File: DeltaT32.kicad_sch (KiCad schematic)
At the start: 35 parts, among them J1 PH2.0, J2 USB_C_Receptacle_USB2.0_16P, J3 SH1.0, Q1 AO3401A, SW1 Boot, SW2 Reset, SW3 SW_SPDT_312, U1 TP4057, U2 MPU-6050, U3 ESP32-C3-MINI-1, U4 AP2112K-3.3

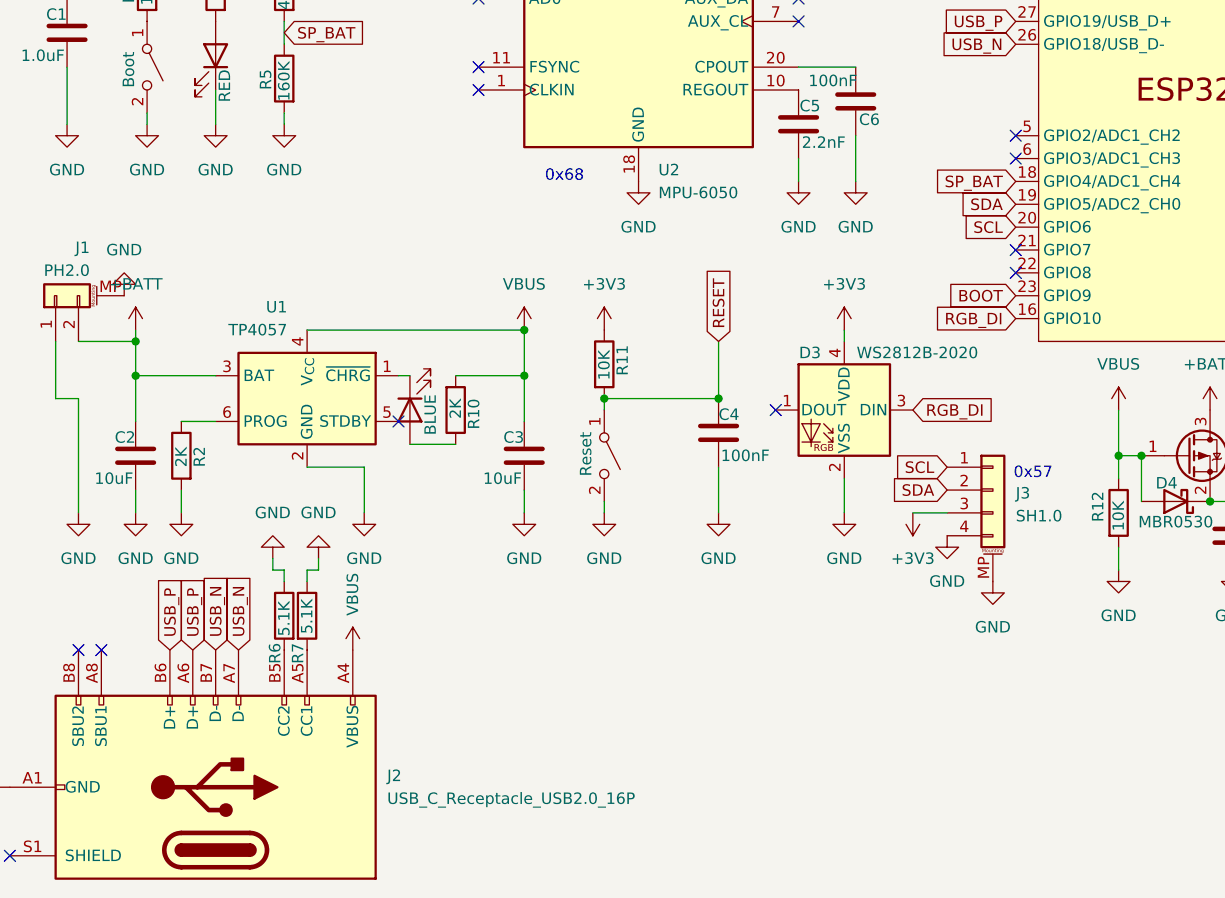
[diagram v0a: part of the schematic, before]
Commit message: Up
Upgrade kicad version
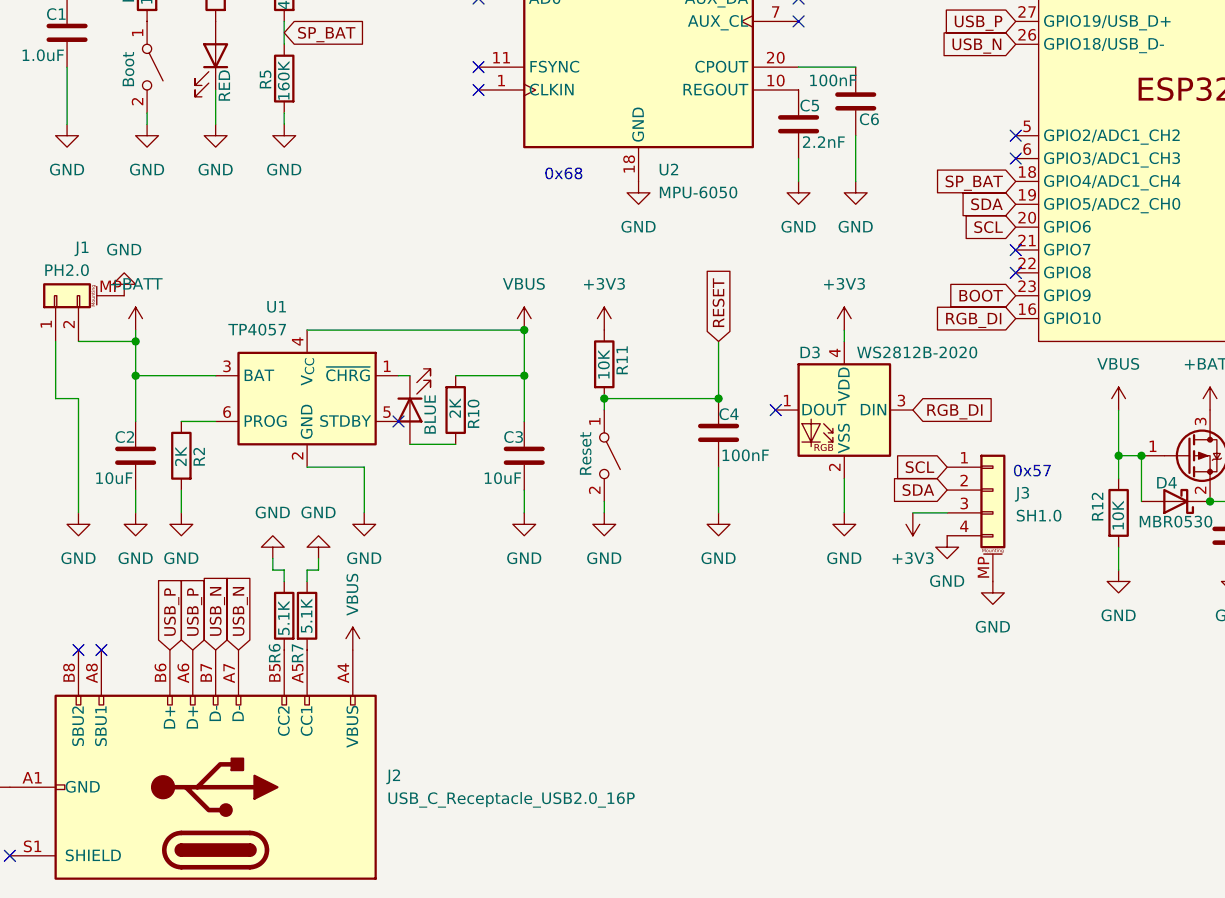
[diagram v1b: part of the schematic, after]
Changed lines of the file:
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@@
 (kicad_sch
-	(version 20231120)
+	(version 20250114)
 	(generator "eeschema")
-	(generator_version "8.0")
+	(generator_version "9.0")
 	(paper "A5")
+	(text_box "0x57"
+		(exclude_from_sim no)
+		(at 129.54 85.09 0)
+		(size 0 0)
+		(margins 0.9525 0.9525 0.9525 0.9525)
+		(stroke
+			(width 0)
+			(type default)
+		)
+		(fill
+			(type none)
+		)
+		(effects
+			(font
+				(size 1.27 1.27)
+			)
+			(justify left top)
+		)
+	)
+	(text_box "0x68"
+		(exclude_from_sim no)
+		(at 77.47 52.07 0)
+		(size 0 0)
+		(margins 0.9525 0.9525 0.9525 0.9525)
+		(stroke
+			(width 0)
+			(type default)
+		)
+		(fill
+			(type none)
+		)
+		(effects
+			(font
+				(size 1.27 1.27)
+			)
+			(justify left top)
+		)
+	)
 	(junction
 		(at 91.44 19.05)
@@
 		)
 	)
-	(text_box "0x57"
-		(exclude_from_sim no)
-		(at 129.54 85.09 0)
-		(size 0 0)
-		(stroke
-			(width 0)
-			(type default)
-		)
-		(fill
-			(type none)
-		)
-		(effects
-			(font
-				(size 1.27 1.27)
-			)
-			(justify left top)
-		)
-	)
-	(text_box "0x68"
-		(exclude_from_sim no)
-		(at 77.47 52.07 0)
-		(size 0 0)
-		(stroke
-			(width 0)
-			(type default)
-		)
-		(fill
-			(type none)
-		)
-		(effects
-			(font
-				(size 1.27 1.27)
-			)
-			(justify left top)
-		)
-	)
 	(global_label "SP_BAT"
 		(shape input)
@@
 		)
 	)
+	(embedded_fonts no)
 )

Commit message: Update Board
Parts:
- removed C1, C7, C8, C9: 1.0uF, Capacitor_SMD:C_0402_1005Metric, symbol Device:C
- removed C2, C3: 10uF, Capacitor_SMD:C_0402_1005Metric, symbol Device:C
- removed C4, C6: 100nF, Capacitor_SMD:C_0402_1005Metric, symbol Device:C
- removed C5: 2.2nF, Capacitor_SMD:C_0603_1608Metric, symbol Device:C
- removed D1: RED, LED_SMD:LED_0402_1005Metric, symbol Device:LED
- removed D2: BLUE, LED_SMD:LED_0402_1005Metric, symbol Device:LED
- removed D3: WS2812B-2020, LED_SMD:LED_WS2812B-2020_PLCC4_2.0x2.0mm, symbol LED:WS2812B-2020
- removed D4: MBR0530, Diode_SMD:D_SOD-123, symbol Diode:MBR0530
- removed J1: PH2.0, Connector_JST:JST_PH_B2B-PH-SM4-TB_1x02-1MP_P2.00mm_Vertical, symbol Connector_Generic_MountingPin:Conn_01x02_MountingPin
- removed J3: SH1.0, Connector_JST:JST_SH_BM04B-SRSS-TB_1x04-1MP_P1.00mm_Vertical, symbol Connector_Generic_MountingPin:Conn_01x04_MountingPin
- removed Q1: AO3401A, Package_TO_SOT_SMD:SOT-23, symbol Transistor_FET:AO3401A
- removed R11, R12: 10K, Resistor_SMD:R_0402_1005Metric, symbol Device:R
- removed SW1: Boot, Button_Switch_SMD:SW_Push_SPST_NO_Alps_SKRK, symbol Switch:SW_SPST
- removed SW2: Reset, Button_Switch_SMD:SW_Push_SPST_NO_Alps_SKRK, symbol Switch:SW_SPST
- removed SW3: SW_SPDT_312, Button_Switch_SMD:SW_SPDT_PCM12, symbol Switch:SW_SPDT_312
- removed U1: TP4057, Package_TO_SOT_SMD:TSOT-23-6, symbol Battery_Management:TP4057
- removed U2: MPU-6050, Sensor_Motion:InvenSense_QFN-24_4x4mm_P0.5mm, symbol Sensor_Motion:MPU-6050
- removed U3: ESP32-C3-MINI-1, PCM_Espressif:ESP32-C3-MINI-1, symbol PCM_Espressif:ESP32-C3-MINI-1
- removed U4: AP2112K-3.3, Package_TO_SOT_SMD:SOT-23-5, symbol Regulator_Linear:AP2112K-3.3
- added C1: 10nF 10V, Capacitor_SMD:C_0402_1005Metric, symbol Device:C_Small
- added C10: 1nF 10V, Capacitor_SMD:C_0402_1005Metric, symbol Device:C_Small
- added C11, C12: DNP, Capacitor_SMD:C_0402_1005Metric, symbol Device:C_Small
- added C2: 100nF 10V, Capacitor_SMD:C_0402_1005Metric, symbol Device:C_Small
- added C3, C4: 1uF 16V, Capacitor_SMD:C_0402_1005Metric, symbol Device:C_Small
- added C5, C6: 4.7uF 16V, Capacitor_SMD:C_0603_1608Metric, symbol Device:C_Small
- added C7, C9: 10uF 16V, Capacitor_SMD:C_0805_2012Metric, symbol Device:C_Small
- added C8: 22pF 50V, Capacitor_SMD:C_0603_1608Metric, symbol Device:C_Small
- added D1: LESD8D3.3CAT5G, Diode_SMD:D_SOD-882, symbol Device:D_TVS
- added D2: WS2812B, LED_SMD:LED_WS2812B-2020_PLCC4_2.0x2.0mm, symbol LED:WS2812B
- added D3: BLUE LED, LED_SMD:LED_0603_1608Metric, symbol Device:LED
- added D4: RED LED, LED_SMD:LED_0603_1608Metric, symbol Device:LED
- added D5, D6, D8: LESD5D5.0CT1G, Diode_SMD:D_SOD-523, symbol Device:D_TVS
- added D7, D9: B5819W, Diode_SMD:D_SOD-123, symbol Device:D_Schottky
- added J1: JST SH 1.0, Connector_JST:JST_SH_SM04B-SRSS-TB_1x04-1MP_P1.00mm_Horizontal, symbol Connector_Generic_MountingPin:Conn_01x04_MountingPin
- added J2: JST PH 2.0, Connector_JST:JST_PH_B2B-PH-K_1x02_P2.00mm_Vertical, symbol Connector_Generic:Conn_01x02
- added L1: 2.2uH 2.2A, Inductor_SMD:L_Bourns-SRN4018, symbol Device:L
- added Q1: DMG3415U, Package_TO_SOT_SMD:SOT-23, symbol Transistor_FET:DMG2301L
- added R14, R7: 10K, Resistor_SMD:R_0402_1005Metric, symbol Device:R
- added R15, R5: 1K, Resistor_SMD:R_0402_1005Metric, symbol Device:R
- added R4, R8: 0R, Resistor_SMD:R_0402_1005Metric, symbol Device:R
- added R6: 470R, Resistor_SMD:R_0402_1005Metric, symbol Device:R
- added R9: 100K, Resistor_SMD:R_0402_1005Metric, symbol Device:R
- added SW1: MSK-12C02-07, Button_Switch_SMD:SW_SPDT_PCM12, symbol Switch:SW_SPDT_312
- added SW2: BOOT, Button_Switch_SMD:SW_Push_SPST_NO_Alps_SKRK, symbol Switch:SW_Push
- added SW3: RESET, Button_Switch_SMD:SW_Push_SPST_NO_Alps_SKRK, symbol Switch:SW_Push
- added TP1: TX, TestPoint:TestPoint_Pad_D1.0mm, symbol Connector:TestPoint
- added TP2: RX, TestPoint:TestPoint_Pad_D1.0mm, symbol Connector:TestPoint
- added TP3: IO3, TestPoint:TestPoint_Pad_D1.0mm, symbol Connector:TestPoint
- added TP4: IO5, TestPoint:TestPoint_Pad_D1.0mm, symbol Connector:TestPoint
- added TP5: IO6, TestPoint:TestPoint_Pad_D1.0mm, symbol Connector:TestPoint
- added U1: ESP32-C3-MINI-1, PCM_Espressif:ESP32-C3-MINI-1, symbol PCM_Espressif:ESP32-C3-MINI-1
- added U2: MCP73831T-2ACI/OT, Package_TO_SOT_SMD:SOT-23-5, symbol Battery_Management:MCP73831-2-OT
- added U3: SY8088, Package_TO_SOT_SMD:SOT-23-5, symbol Rust_Board:SY8088
- added Y1: 32.768Hz, Crystal:Crystal_SMD_3215-2Pin_3.2x1.5mm, symbol Device:Crystal
- J3: renamed from J2; value USB_C_Receptacle_USB2.0_16P -> USB C 16P; footprint Connector_USB:USB_C_Receptacle_GCT_USB4110 -> Connector_USB:USB_C_Receptacle_GCT_USB4105-xx-A_16P_TopMnt_Horizontal
- R1: value 10K -> 0R
- R10: value 2K -> 22K1
- R11: renamed from R6; value 5.1K -> 5K1
- R12: renamed from R7; value 5.1K -> 5K1
- R13: value 10K -> 100K
- R2, R3: value 2K -> 10K
- renumbered R4 to R16, R5 to R17
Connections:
- net +BATT: now also C6.1, J2.2 (Pin_2), Q1.3 (D), U2.3 (VBAT)
- net BOOT: now also C10.2, R14.2, SW3.1, U1.23 (GPIO9); no longer R1.1
- net GND: now also R10.2, R13.2, R3.2, C1.2, C10.1, C11.2, C12.2, C2.2, C3.2, C4.2, C5.1, C6.2, C7.2, C9.2, D1.2 (A2), D2.3 (VSS), D4.1 (K), D5.2 (A2), D6.2 (A2), D8.2 (A2), J1.1 (Pin_1), J2.1 (Pin_1), R8.1, SW2.2, SW3.2, U1.1 (GND), U1.11 (GND), U1.14 (GND), U1.2 (GND), U1.36 (GND), U1.37 (GND), U1.38 (GND), U1.39 (GND), U1.40 (GND), U1.41 (GND), U1.42 (GND), U1.43 (GND), U1.44 (GND), U1.45 (GND), U1.46 (GND), U1.47 (GND), U1.48 (GND), U1.49 (GND), U1.50 (GND), U1.51 (GND), U1.52 (GND), U1.53 (GND), U2.2 (VSS), U3.2 (GND); no longer R2.2
- net SCL: now also J1.3 (Pin_3), U1.22 (GPIO8)
- net SDA: now also J1.4 (Pin_4), U1.16 (GPIO10)
- net VBUS: now also R13.1, C5.2, D3.2 (A), D7.1 (K), D9.2 (A), Q1.1 (G), U2.4 (VDD); no longer J3.A4 (VBUS), J3.A9 (VBUS), J3.B4 (VBUS), J3.B9 (VBUS), R10.2
- net +3.3V: now reaches R2.1
- net +3.3V: now also C1.1, C2.1, C3.1, D1.1 (A1), D2.1 (VDD), J1.2 (Pin_2), R14.1, SW1.1 (B), U1.3 (3V3)
- net at R1.2: now also U1.6 (GPIO3/ADC1_CH3)
- net at R10.1: now also C8.2, R9.2, U3.5 (FB)
- net at J3.S1 (SHIELD): now also R8.2
- net +3V3: no longer names the net of R3.1
- net +3V3: now also U2.5 (PROG)
- net SP_BAT renamed IO3
- net IO3: now also R1.1
- net USB_N renamed USB_D-
- net USB_D-: now also D6.1 (A1), U1.26 (GPIO18/USB_D-)
- net USB_P renamed USB_D+
- net USB_D+: now also D5.1 (A1), U1.27 (GPIO19/USB_D+)
- new net: TP3.1, U1.18 (GPIO4/ADC1_CH4)
- new net: R5.1, U2.1 (STAT)
- new net: D3.1 (K), R5.2
- new net: D7.2 (A), D8.1 (A1), J3.A4 (VBUS), J3.A9 (VBUS), J3.B4 (VBUS), J3.B9 (VBUS)
- new net: D2.4 (DIN), R4.2
- new net: TP4.1, U1.19 (GPIO5/ADC2_CH0)
- new net: TP5.1, U1.20 (GPIO6)
- new net: TP2.1, U1.30 (GPIO20/U0RXD)
- new net: TP1.1, U1.31 (GPIO21/U0TXD)
- new net: D4.2 (A), R6.2
- new net +5V: C7.1, D9.1 (K), Q1.2 (S), R7.1, U3.4 (IN)
- new net Buck_Coil: L1.1, U3.3 (LX)
- new net CHIP_PU: C4.1, R2.2, SW2.1, U1.8 (EN/CHIP_PU)
- new net EN: R7.2, U3.1 (EN)
- new net IO0: C11.1, R15.1, U1.12 (GPIO0/ADC1_CH0/XTAL_32K_P), Y1.1
- new net IO1: C12.1, R15.2, U1.13 (GPIO1/ADC1_CH1/XTAL_32K_N), Y1.2
- new net IO2: R4.1, U1.5 (GPIO2/ADC1_CH2)
- new net IO7: R6.1, U1.21 (GPIO7)
- new net Switch: C8.1, C9.1, L1.2, R9.1, SW1.2 (C)
- no-connect marks 20 -> 5
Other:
- added sheet BMI (BMI.kicad_sch)
- added sheet ICM20948 (ICM20948.kicad_sch)
- added sheet MPU6050 (MPU6050.kicad_sch)
- added sheet MPU9250 (MPU9250.kicad_sch)
- note added: "Buck Converter 3V3 Rails"
- note added: "Buttons (Reset & Boot)"
- note added: "Charge Management Controller"
- note added: "ESP32-C3-MINI-1 Module"
- note added: "IMU & Heart Rate Sensor"
- note added: "IMU Default : 0x68 (1101000b) Alternative : 0x69 (1101001b) Heart-Rate Sensor Default : 0x57 (1010111b)"
- note added: "LED RED GPIO7 RGB GPIO2"
- note added: "LF Crystal 32.768Hz Do Not Populate"
- note added: "USB & Battery Switch"
- note added: "USB Type-C Connector"
- note added: "Voltage Divider"
- title: (none) -> DeltaT32
- moved on the sheet: J3, R11, R12, R16, R17

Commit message: Update Board
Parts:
- J2: footprint Connector_JST:JST_PH_B2B-PH-K_1x02_P2.00mm_Vertical -> Connector_JST:JST_PH_S2B-PH-K_1x02_P2.00mm_Horizontal
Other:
- removed sheet ICM20948
- removed sheet MPU6050
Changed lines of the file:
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@@
 	(polyline
 		(pts
-			(xy 64.77 102.87) (xy 64.77 156.21)
+			(xy 64.77 102.87) (xy 64.77 139.7)
 		)
 		(stroke
@@
 	(polyline
 		(pts
-			(xy 12.7 156.21) (xy 12.7 102.87)
+			(xy 12.7 139.7) (xy 12.7 102.87)
 		)
 		(stroke
@@
 	(polyline
 		(pts
-			(xy 64.77 156.21) (xy 12.7 156.21)
+			(xy 64.77 139.7) (xy 12.7 139.7)
 		)
 		(stroke
@@
 			"AAAAAAAAAAAAAAAAAAAAAAAAAAAAAAAAAAAAAAAAAAAAAAAAAAAAAADwAAAAAAAAAASzwJEABACA"
 			"0JgX/psBAACAvxj+mwEAAIC/GP6bAQAAABAAAAAAAAAAAAAAAAAAAICvGP6bAQAAAAAAAAAAAAAA"
-			"AAAAAAAAAAAAAAAAAAAAoK8Y/psBAAAAAAAAAAAAAAAAAAAAAAAAAAAAAAAAAADArxj+mw=="
+			"AAAAAAAAAAAAAAAAAAAAoK8Y/psBAAAAAAAAAAAAAAAAAAAAAAAAAAAAAAAAAADArxj+mwAAAAAA"
+			"AAAAAAAAAAAAAAAAAAAAAAAAAAAAAAAAAAAAAAAAAAAAAAAAAAAAAAAAAAAAAAAAAAAAAAAAAAAA"
+			"AAAAAAAAAAAAAAAAAAAAAAAAAAAAAAAAAAAAAAAAAAAAAAAAAAAAAAAAAAAAAAAAAAAAAAAAAAAA"
+			"AAAAAAAAAAAAAAAAAAAAAAAAAAAAAAAAAAAAAAAAAAAAAAAAAAAAAAAAAAAAAAAAAAAAAAAAAAAA"
+			"AAAAAAAAAAAAAAAAAAAAAAAAAAAAAAAAAAAAAAAAAAAAAAAAAAAAAAAAAAAAAAAAAAAAAAAAAAAA"
+			"AAAAAAAAAAAAAAAAAAAAAAAAAAAAAAAAAAAAAAAAAAAAAAAAAAAAAAAAAAAAAAAAAAAAAAAAAAAA"
+			"AAAAAAAAAAAAAAAAAAAAAAAAAAAAAAAAAAAAAAAAAAAAAAAAAAAAAAAAAAAAAAAAAAAAAAAAAAAA"
+			"AAAAAAAAAAAAAAAAAAAAAAAAAAAAAAAAAAAAAAAAAAAAAAAAAAAAAAAAAAAAAAAAAAAAAAAAAAAA"
+			"AAAAAAAAAAAAAAAAAAAAAAAAAAAAAAAAAAAAAAAAAAAAAAAAAAAAAAAAAAAAAAAAAAAAAAAAAAAA"
+			"AAAAAAAAAAAAAAAAAAAAAAAAAAAAAAAAAAAAAAAAAAAAAAAAAAAAAAAAAAAAAAAAAAAAAAAAAAAA"
+			"AAAAAAAAAAAAAAAAAAAAAAAAAAAAAAAAAAAAAAAAAAAAAAAAAAAAAAAAAAAAAAAAAAAAAAAAAAAA"
+			"AAAAAAAAAAAAAAAAAAAAAAAAAAAAAAAAAAAAAAAAAAAAAAAAAAAAAAAAAAAAAAAAAAAAAAAAAAAA"
+			"AAAAAAAAAAAAAAAAAAAAAAAAAAAAAAAAAAAAAAAAAAAAAAAAAAAAAAAAAAAAAAAAAAAAAAAAAAAA"
+			"AAAAAAAAAAAAAAAAAAAAAAAAAAAAAAAAAAAAAAAAAAAAAAAAAAAAAAAAAAAAAAAAAAAAAAAAAAAA"
+			"AAAAAAAAAAAAAAAAAAAAAAAAAAAAAAAAAAAAAAAAAAAAAAAAAAAAAAAAAAAAAAAAAAAAAAAAAAAA"
+			"AAAAAAAAAAAAAAAAAAAAAAAAAAAAAAAAAAAAAAAAAAAAAAAAAAAAAAAAAAAAAAAAAAAAAAAAAAAA"
+			"AAAAAAAAAAAAAAAAAAAAAAAAAAAAAAAAAAAAAAAAAAAAAAAAAAAAAAAAAAAAAAAAAAAAAAAAAAAA"
+			"AAAAAAAAAAAAAAAAAAAAAAAAAAAAAAAAAAAAAAAAAAAAAAAAAAAAAAAAAAAAAAAAAAAAAAAAAAAA"
+			"AAAAAAAAAAAAAAAAAAAAAAAAAAAAAAAAAAAAAAAAAAAAAAAAAAAAAAAAAAAAAAAAAAAAAAAAAAAA"
+			"AAAAAAAAAAAAAAAAAAAAAAAAAAAAAAAAAAAAAAAAAAAAAAAAAAAAAAAAAAAAAAAAAAAAAAAAAAAA"
+			"AAAAAAAAAAAAAAAAAAAAAAAAAAAAAAAAAAAAAAAAAAAAAAAAAAAAAAAAAAAAAAAAAAAAAAAAAAAA"
+			"AAAAAAAAAAAAAAAAAAAAAAAAAAAAAAAAAAAAAAAAAAAAAAAAAAAAAAAAAAAAAAAAAAAAAAAAAAAA"
+			"AAAAAAAAAAAAAAAAAAAAAAAAAAAAAAAAAAAAAAAAAAAAAAAAAAAAAAAAAAAAAAAAAAAAAAAAAAAA"
+			"AAAAAAAAAAAAAAAAAAAAAAAAAAAAAAAAAAAAAAAAAAAAAAAAAAAAAAAAAAAAAAAAAAAAAAAAAAAA"
+			"AAAAAAAAAAAAAAAAAAAAAAAAAAAAAAAAAAAAAAAAAAAAAAAAAAAAAAAAAAAAAAAAAAAAAAAAAAAA"
+			"AAAAAAAAAAAAAAAAAAAAAAAAAAAAAAAAAAAAAAAAAAAAAAAAAAAAAAAAAAAAAAAAAAAAAAAAAAAA"
+			"AAAAAAAAAAAAAAAAAAAAAAAAAAAAAAAAAAAAAAAAAAAAAAAAAAAAAAAAAAAAAAAAAAAAAAAAAAAA"
+			"AAAAAAAAAAAAAAAAAAAAAAAAAAAAAAAAAAAAAAAAAAAAAAAAAAAAAAAAAAAAAAAAAAAAAAAAAAAA"
+			"AAAAAAAAAAAAAAAAAAAAAAAAAAAAAAAAAAAAAAAAAAAAAAAAAAAAAAAAAAAAAAAAAAAAAAAAAAAA"
+			"AAAAAAAAAAAAAAAAAAAAAAAAAAAAAAAAAAAAAAAAAAAAAAAAAAAAAAAAAAAAAAAAAAAAAAAAAAAA"
+			"AAAAAAAAAAAAAAAAAAAAAAAAAAAAAAAAAAAAAAAAAAAAAAAAAAAAAAAAAAAAAAAAAAAAAAAAAAAA"
+			"AAAAAAAAAAAAAAAAAAAAAAAAAAAAAAAAAAAAAAAAAAAAAAAAAAAAAAAAAAAAAAAAAAAAAAAAAAAA"
+			"AAAAAAAAAAAAAAAAAAAAAAAAAAAAAAAAAAAAAAAAAAAAAAAAAAAAAAAAAAAAAAAAAAAAAAAAAAAA"
+			"AAAAAAAAAAAAAAAAAAAAAAAAAAAAAAAAAAAAAAAAAAAAAAAAAAAAAAAAAAAAAAAAAAAAAAAAAAAA"
+			"AAAAAAAAAAAAAAAAAAAAAAAAAAAAAAAAAAAAAAAAAAAAAAAAAAAAAAAAAAAAAAAAAAAAAAAAAAAA"
+			"AAAAAAAAAAAAAAAAAAAAAAAAAAAAAAAAAAAAAAAAAAAAAAAAAAAAAAAAAAAAAAAAAAAAAAAAAAAA"
+			"AAAAAAAAAAAAAAAAAAAAAAAAAAAAAAAAAAAAAAAAAAAAAAAAAAAAAAAAAAAAAAAAAAAAAP///wQA"
+			"AAD4/////////3gDAAAAAAAA/////wQAAAD4/////////wAAAAAAAAAA/////wQAAAD4////////"
+			"/94AAAAAAAAA/////wQAAAD4/////////98CAAAAAAAA/////wQAAAD4/////////2gBAAAAAAAA"
+			"/////wQAAAD4/////////wAAAAAAAAAA/////wQAAAD4/////////xsDAAAAAAAA/////wQAAAD4"
+			"/////////70AAAAAAAAA/////wQAAAD4/////////6IBAAAAAAAA/////wQAAAD4/////////9gA"
+			"AAAAAAAA/////wQAAAD4/////////w8BAAAAAAAA/////wQAAAD4/////////0EAAAAAAAAA////"
+			"/wQAAAD4/////////5oAAAAAAAAA/////wQAAAD4/////////wAAAAAAAAAA/////wQAAAD4////"
+			"/////wAAAAAAAAAA/////wQAAAD4/////////wAAAAAAAAAA/////wQAAAD4/////////5gAAAAA"
+			"AAAA/////wQAAAD4/////////wAAAAAAAAAA/////wQAAAD4/////////9ICAAAAAAAA/////wQA"
+			"AAD4/////////18AAAAAAAAA/////wQAAAD4/////////9kBAAAAAAAA/////wQAAAD4////////"
+			"/xwBAAAAAAAA/////wQAAAD4/////////0sAAAAAAAAA/////wQAAAD4/////////wAAAAAAAAAA"
+			"/////wQAAAD4/////////48AAAAAAAAA/////wQAAAD4/////////wAAAAAAAAAA/////wQAAAD4"
+			"/////////wAAAAAAAAAA/////wQAAAD4/////////wAAAAAAAAAA/////wQAAAD4/////////10A"
+			"AAAAAAAA/////wQAAAD4/////////5wAAAAAAAAA/////wQAAAD4/////////9gCAAAAAAAA////"
+			"/wQAAAD4/////////wAAAAAAAAAA/////wQAAAD4/////////wAAAAAAAAAA/////wQAAAD4////"
+			"/////wAAAAAAAAAA/////wQAAAD4/////////wAAAAAAAAAA/////wQAAAD4/////////wAAAAAA"
+			"AAAA/////wQAAAD4/////////zoBAAAAAAAA/////wQAAAD4/////////0sCAAAAAAAA/////wQA"
+			"AAD4/////////8wAAAAAAAAA/////wQAAAD4//////////kCAAAAAAAA/////wQAAAD4////////"
+			"/9QBAAAAAAAA/////wQAAAD4/////////wAAAAAAAAAA/////wQAAAD4/////////wAAAP9aWlr/"
+			"Wlpa/1paWv9aWlr/Wlpa/1paWv9aWlr/Wlpa/1paWv9aWlr/Wlpa/1paWv9aWlr/Wlpa/1paWv9a"
+			"Wlr/Wlpa/1paWv9aWlr/Wlpa/1paWv9aWlr/Wlpa/1paWv9aWlr/Wlpa/1paWv9aWlr/Wlpa/1pa"
+			"Wv9aWlr/Wlpa/1paWv9aWlr/Wlpa/1paWv9aWlr/Wlpa/1paWv9aWlr/Wlpa/1paWv9aWlr/Wlpa"
+			"/1paWv9aWlr/Wlpa/1paWv9aWlr/Wlpa/1paWv9aWlr/Wlpa/1paWv+inIz/0MWs/9DFrP/Qxaz/"
+			"0MWs/9DFrP/Qxaz/0MWs/9DFrP/Qxaz/0MWs/9DFrP/Qxaz/0MWs/9DFrP/Qxaz/0MWs/9DFrP/Q"
+			"xaz/0MWs/9DFrP/Qxaz/0MWs/9DFrP/Qxaz/0MWs/9DFrP/Qxaz/0MWs/9DFrP/Qxaz/0MWs/9DF"
+			"rP/Qxaz/0MWs/9DFrP/Qxaz/0MWs/9DFrP/Qxaz/0MWs/9DFrP/Qxaz/0MWs/9DFrP/Qxaz/0MWs"
+			"/9DFrP/Qxaz/0MWs/9DFrP/Qxaz/0MWs/9DFrP/Qxaz/0MWs/9DFrP/Qxaz/0MWs/9DFrP/Qxaz/"
+			"0MWs/9DFrP/Qxaz/0MWs/9DFrP/Qxaz/0MWs/9DFrP/Qxaz/0MWs/9DFrP/Qxaz/0MWs/9DFrP/Q"
+			"xaz/0MWs/9DFrP/Qxaz/0MWs/9DFrP/Qxaz/0MWs/9DFrP/Qxaz/0MWs/9DFrP/Qxaz/0MWs/9DF"
+			"rP/Qxaz/0MWs/9DFrP/Qxaz/0MWs/9DFrP/Qxaz/0MWs/9DFrP/Qxaz/0MWs/9DFrP/Qxaz/0MWs"
+			"/9DFrP/Qxaz/0MWs/9DFrP/Qxaz/0MWs/9DFrP/Qxaz/0MWs/9DFrP/Qxaz/0MWs/9DFrP/Qxaz/"
+			"0MWs/9DFrP/Qxaz/0MWs/9DFrP/Qxaz/0MWs/9DFrP/Qxaz/vbOd/zMzM/8zMzP/MzMz/zMzM/8z"
+			"MzP/MzMz/zMzM/8zMzP/MzMz/zMzM/8zMzP/MzMz/zMzM/8zMzP/MzMz/zMzM/8zMzP/MzMz/zMz"
+			"M/8zMzP/MzMz/zMzM/8zMzP/SUdE/6CZh//Qxaz/0MWs/9DFrP/Qxaz/0MWs/9DFrP/Qxaz/0MWs"
+			"/9DFrP/Qxaz/0MWs/9DFrP/Qxaz/0MWs/9DFrP/Topv/4RBS/9wfV//gFlT/0L+p/9DFrP/Qxaz/"
+			"0MWs/9DFrP/Qxaz/0MWs/9DFrP/Qxaz/0MWs/9DFrP/Qxaz/0MWs/9DFrP/Qxaz/0MWs/9DFrP/Q"
+			"xaz/0MWs/9DFrP/Kv6j/bWtn/1paWv9aWlr/Wlpa/1paWv9aWlr/Wlpa/1paWv9aWlr/Wg=="
 		)
 	)
@@
 			)
 		)
-		(property "Footprint" "Connector_JST:JST_PH_B2B-PH-K_1x02_P2.00mm_Vertical"
+		(property "Footprint" "Connector_JST:JST_PH_S2B-PH-K_1x02_P2.00mm_Horizontal"
 			(at 135.89 113.03 0)
 			(effects
@@
 	)
 	(sheet
-		(at 13.97 123.19)
-		(size 12.7 10.16)
-		(exclude_from_sim no)
-		(in_bom yes)
-		(on_board yes)
-		(dnp no)
-		(fields_autoplaced yes)
-		(stroke
-			(width 0.1524)
-			(type solid)
-		)
-		(fill
-			(color 0 0 0 0.0000)
-		)
-		(property "Sheetname" "ICM20948"
-			(at 13.97 122.4784 0)
-			(effects
-				(font
-					(size 1.27 1.27)
-				)
-				(justify left bottom)
-			)
-		)
-		(property "Sheetfile" "ICM20948.kicad_sch"
-			(at 13.97 133.9346 0)
-			(effects
-				(font
-					(size 1.27 1.27)
-				)
-				(justify left top)
-			)
-		)
-		(pin "SDA" bidirectional
-			(at 26.67 127 0)
-			(effects
-				(font
-					(size 1.27 1.27)
-				)
-				(justify right)
-			)
-		)
-		(pin "SCL" bidirectional
-			(at 26.67 129.54 0)
-			(effects
-				(font
-					(size 1.27 1.27)
-				)
-				(justify right)
-			)
-		)
-		(instances
-			(project "DeltaT32"
-				(path "/418142f0-ca8b-4509-a0db-baeccce9fb59"
-					(page "2")
-				)
-			)
-		)
-	)
-	(sheet
-		(at 39.37 139.7)
-		(size 12.7 10.16)
-		(exclude_from_sim no)
-		(in_bom yes)
-		(on_board yes)
-		(dnp no)
-		(fields_autoplaced yes)
-		(stroke
-			(width 0.1524)
-			(type solid)
-		)
-		(fill
-			(color 0 0 0 0.0000)
-		)
-		(property "Sheetname" "MPU6050"
-			(at 39.37 138.9884 0)
-			(effects
-				(font
-					(size 1.27 1.27)
-				)
-				(justify left bottom)
-			)
-		)
-		(property "Sheetfile" "MPU6050.kicad_sch"
-			(at 39.37 150.4446 0)
-			(effects
-				(font
-					(size 1.27 1.27)
-				)
-				(justify left top)
-			)
-		)
-		(pin "SDA" bidirectional
-			(at 52.07 143.51 0)
-			(effects
-				(font
-					(size 1.27 1.27)
-				)
-				(justify right)
-			)
-		)
-		(pin "SCL" bidirectional
-			(at 52.07 146.05 0)
-			(effects
-				(font
-					(size 1.27 1.27)
-				)
-				(justify right)
-			)
-		)
-		(instances
-			(project "DeltaT32"
-				(path "/418142f0-ca8b-4509-a0db-baeccce9fb59"
-					(page "5")
-				)
-			)
-		)
-	)
-	(sheet
 		(at 39.37 123.19)
 		(size 12.7 10.16)
@@
 	)
 	(sheet
-		(at 13.97 139.7)
+		(at 13.97 123.19)
 		(size 12.7 10.16)
 		(exclude_from_sim no)
@@
 		)
 		(property "Sheetname" "MPU9250"
-			(at 13.97 138.9884 0)
+			(at 13.97 122.4784 0)
 			(effects
 				(font
@@
 		)
 		(property "Sheetfile" "MPU9250.kicad_sch"
-			(at 13.97 150.4446 0)
+			(at 13.97 133.9346 0)
 			(effects
 				(font
@@
 		)
 		(pin "SDA" bidirectional
-			(at 26.67 143.51 0)
+			(at 26.67 127 0)
 			(effects
 				(font
@@
 		)
 		(pin "SCL" bidirectional
-			(at 26.67 146.05 0)
+			(at 26.67 129.54 0)
 			(effects
 				(font
